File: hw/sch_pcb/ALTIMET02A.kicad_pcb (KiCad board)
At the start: 2 copper layers, 40.1 x 19.8 mm, 14 parts, among them IC1 MS561101BA03-50, J1 HEADER_2x03_PARALLEL, J2 HEADER_2x03, J3 HEADER_2x05_PARALLEL

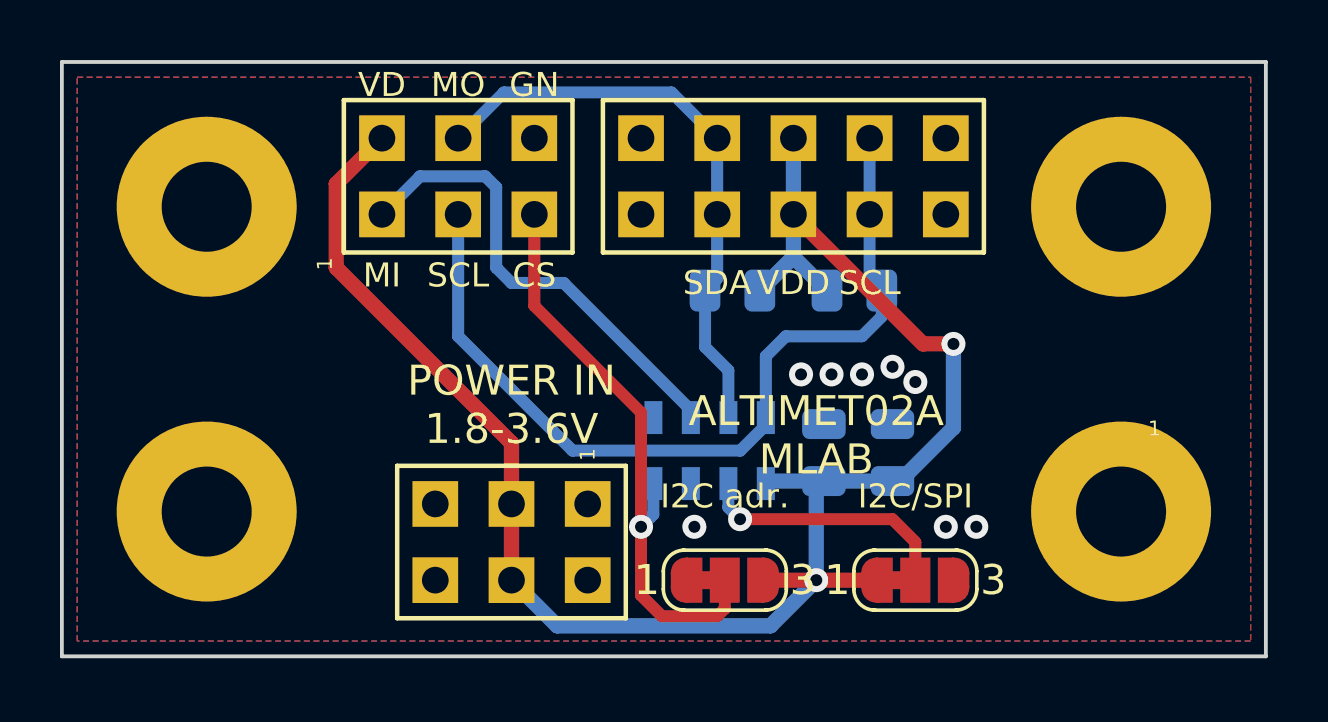
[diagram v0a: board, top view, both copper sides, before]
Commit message: Layout and silkscreen improvements.
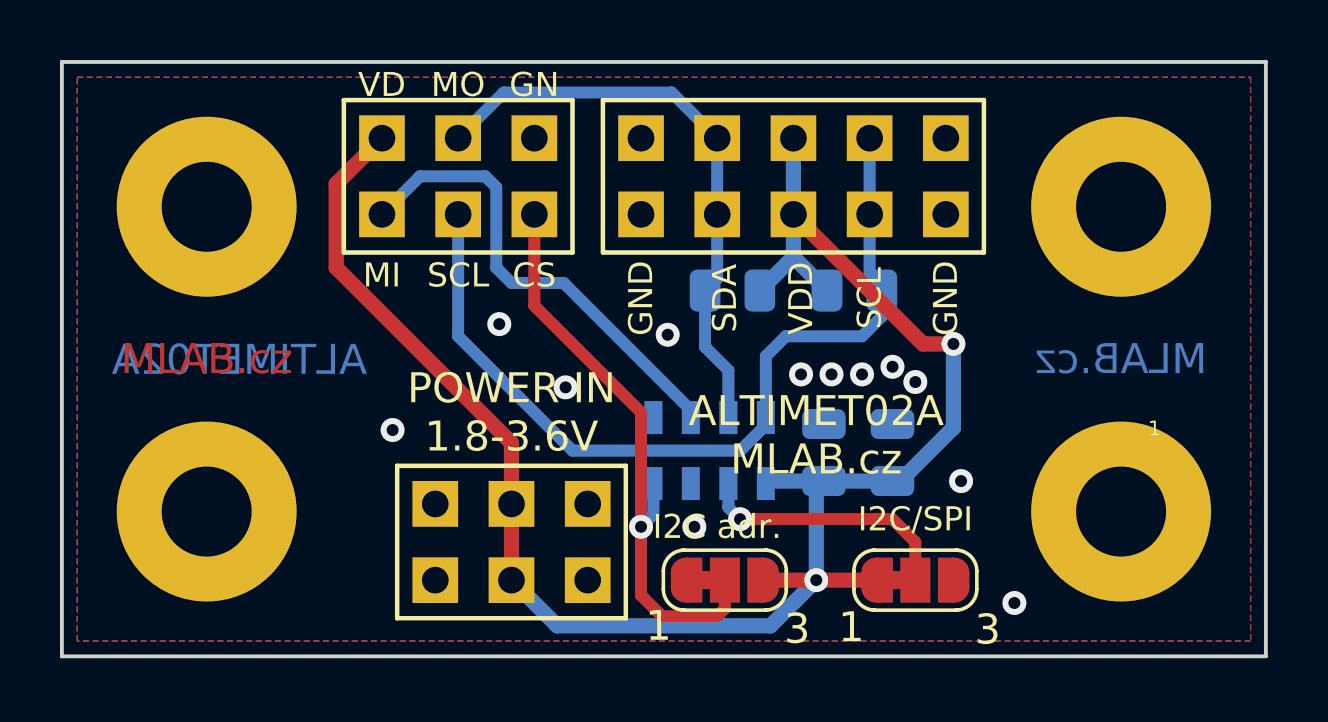
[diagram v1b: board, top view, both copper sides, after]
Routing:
- net GND: vias 8 -> 12
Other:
- board text added: "ALTIMET02A"
- board text added: "ALTIMET02A MLAB.cz"
- board text added: "GND"
- board text added: "MLAB.cz"
- board text removed: "ALTIMET02A MLAB"
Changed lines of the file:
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@@
       (effects (font (size 1.5 1.5) (thickness 0.15)))
-    )
-    (fp_text user "1" (at -2.921 -4.442928 90) (layer "F.SilkS")
-      (effects (font (size 0.5 0.5) (thickness 0.05)))
     )
     (fp_line (start -2.54 3.81) (end -2.54 -3.81) (layer "F.SilkS") (width 0.15))
@@
       (effects (font (size 1 1) (thickness 0.15)))
     )
-    (fp_text user "3" (at 2.6 0) (layer "F.SilkS")
-      (effects (font (size 1 1) (thickness 0.15)))
-    )
-    (fp_text user "1" (at -2.6 0) (layer "F.SilkS")
+    (fp_text user "3" (at 2.413 1.6256) (layer "F.SilkS")
+      (effects (font (size 1 1) (thickness 0.15)))
+    )
+    (fp_text user "1" (at -2.2098 1.524) (layer "F.SilkS")
       (effects (font (size 1 1) (thickness 0.15)))
     )
@@
       (effects (font (size 1 1) (thickness 0.15)))
     )
-    (fp_text user "1" (at -2.6 0) (layer "F.SilkS")
-      (effects (font (size 1 1) (thickness 0.15)))
-    )
-    (fp_text user "3" (at 2.6 0) (layer "F.SilkS")
+    (fp_text user "1" (at -2.1336 1.5748) (layer "F.SilkS")
+      (effects (font (size 1 1) (thickness 0.15)))
+    )
+    (fp_text user "3" (at 2.413 1.651) (layer "F.SilkS")
       (effects (font (size 1 1) (thickness 0.15)))
     )
@@
       (effects (font (size 1.5 1.5) (thickness 0.15)))
     )
-    (fp_text user "1" (at -2.921 -2.54 90) (layer "F.SilkS")
+    (fp_text user "1" (at -2.921 -2.54 90) (layer "F.SilkS") hide
       (effects (font (size 0.5 0.5) (thickness 0.05)))
     )
@@
     (property "Sheetname" "")
     (attr smd)
-    (fp_text reference "IC1" (at 0 0 90) (layer "B.SilkS")
+    (fp_text reference "IC1" (at 1.4224 -3.4036 90) (layer "B.SilkS")
       (effects (font (size 1.27 1.27) (thickness 0.254)) (justify mirror))
     )
@@
   (gr_line (start 152.146 116.586) (end 112.014 116.586) (layer "Edge.Cuts") (width 0.127))
   (gr_line (start 152.146 96.774) (end 152.146 116.586) (layer "Edge.Cuts") (width 0.127))
+  (gr_text "MLAB.cz" (at 116.84 106.68) (layer "F.Cu")
+    (effects (font (size 1 1) (thickness 0.15)))
+  )
+  (gr_text "MLAB.cz" (at 147.32 106.68) (layer "B.Cu")
+    (effects (font (size 1 1) (thickness 0.15)) (justify mirror))
+  )
+  (gr_text "ALTIMET02A" (at 117.9322 106.7054) (layer "B.Cu")
+    (effects (font (size 1 1) (thickness 0.15)) (justify mirror))
+  )
   (gr_text "GN" (at 127.762 97.536) (layer "F.SilkS")
     (effects (font (size 0.8 0.8) (thickness 0.15)))
@@
     (effects (font (size 0.8 0.8) (thickness 0.15)))
   )
-  (gr_text "SDA" (at 133.858 104.14) (layer "F.SilkS")
+  (gr_text "SDA" (at 134.112 104.648 90) (layer "F.SilkS")
     (effects (font (size 0.8 0.8) (thickness 0.15)))
   )
@@
     (effects (font (size 0.8 0.8) (thickness 0.15)))
   )
-  (gr_text "SCL" (at 138.938 104.14) (layer "F.SilkS")
-    (effects (font (size 0.8 0.8) (thickness 0.15)))
-  )
-  (gr_text "VDD" (at 136.398 104.14) (layer "F.SilkS")
-    (effects (font (size 0.8 0.8) (thickness 0.15)))
-  )
-  (gr_text "POWER IN\n1.8-3.6V" (at 127 108.204) (layer "F.SilkS")
+  (gr_text "GND" (at 141.478 104.648 90) (layer "F.SilkS")
+    (effects (font (size 0.8 0.8) (thickness 0.15)))
+  )
+  (gr_text "SCL" (at 138.938 104.648 90) (layer "F.SilkS")
+    (effects (font (size 0.8 0.8) (thickness 0.15)))
+  )
+  (gr_text "VDD" (at 136.652 104.648 90) (layer "F.SilkS")
+    (effects (font (size 0.8 0.8) (thickness 0.15)))
+  )
+  (gr_text "POWER IN\n1.8-3.6V" (at 127 108.458) (layer "F.SilkS")
     (effects (font (size 1 1) (thickness 0.15)))
   )
-  (gr_text "I2C adr." (at 134.112 111.252) (layer "F.SilkS")
+  (gr_text "I2C adr." (at 133.858 112.268) (layer "F.SilkS")
     (effects (font (size 0.8 0.8) (thickness 0.15)))
   )
@@
     (effects (font (size 0.8 0.8) (thickness 0.15)))
   )
-  (gr_text "ALTIMET02A\nMLAB" (at 137.16 109.22) (layer "F.SilkS")
+  (gr_text "GND" (at 131.318 104.648 90) (layer "F.SilkS")
+    (effects (font (size 0.8 0.8) (thickness 0.15)))
+  )
+  (gr_text "ALTIMET02A\nMLAB.cz" (at 137.16 109.22) (layer "F.SilkS")
     (effects (font (size 1 1) (thickness 0.15)))
   )
@@
     (effects (font (size 0.8 0.8) (thickness 0.15)))
   )
-  (gr_text "I2C/SPI" (at 140.462 111.252) (layer "F.SilkS")
+  (gr_text "I2C/SPI" (at 140.462 112.014) (layer "F.SilkS")
     (effects (font (size 0.8 0.8) (thickness 0.15)))
   )
@@
   (segment (start 134.229 111.623) (end 134.229 110.828) (width 0.4) (layer "B.Cu") (net 5))
   (segment (start 134.62 112.014) (end 134.229 111.623) (width 0.4) (layer "B.Cu") (net 5))
-  (via (at 142.494 112.268) (size 0.8) (drill 0.4) (layers "F.Cu" "B.Cu") (free) (net 6))
+  (via (at 126.5936 105.5116) (size 0.8) (drill 0.4) (layers "F.Cu" "B.Cu") (free) (net 6))
+  (via (at 123.0376 109.0422) (size 0.8) (drill 0.4) (layers "F.Cu" "B.Cu") (free) (net 6))
+  (via (at 141.986 110.744) (size 0.8) (drill 0.4) (layers "F.Cu" "B.Cu") (free) (net 6))
+  (via (at 128.8034 107.6198) (size 0.8) (drill 0.4) (layers "F.Cu" "B.Cu") (free) (net 6))
   (via (at 133.096 112.268) (size 0.8) (drill 0.4) (layers "F.Cu" "B.Cu") (free) (net 6))
   (via (at 136.652 107.188) (size 0.8) (drill 0.4) (layers "F.Cu" "B.Cu") (free) (net 6))
   (via (at 140.462 107.442) (size 0.8) (drill 0.4) (layers "F.Cu" "B.Cu") (free) (net 6))
+  (via (at 132.207 105.8672) (size 0.8) (drill 0.4) (layers "F.Cu" "B.Cu") (free) (net 6))
   (via (at 138.684 107.188) (size 0.8) (drill 0.4) (layers "F.Cu" "B.Cu") (free) (net 6))
   (via (at 137.668 107.188) (size 0.8) (drill 0.4) (layers "F.Cu" "B.Cu") (free) (net 6))
-  (via (at 141.478 112.268) (size 0.8) (drill 0.4) (layers "F.Cu" "B.Cu") (free) (net 6))
+  (via (at 143.764 114.808) (size 0.8) (drill 0.4) (layers "F.Cu" "B.Cu") (free) (net 6))
   (via (at 139.7 106.934) (size 0.8) (drill 0.4) (layers "F.Cu" "B.Cu") (free) (net 6))
   (segment (start 139.3425 105.2595) (end 138.684 105.918) (width 0.4) (layer "B.Cu") (net 7))

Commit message: power header deleted, i2c/spi solder jumper moved to the back side, i2c addr. added
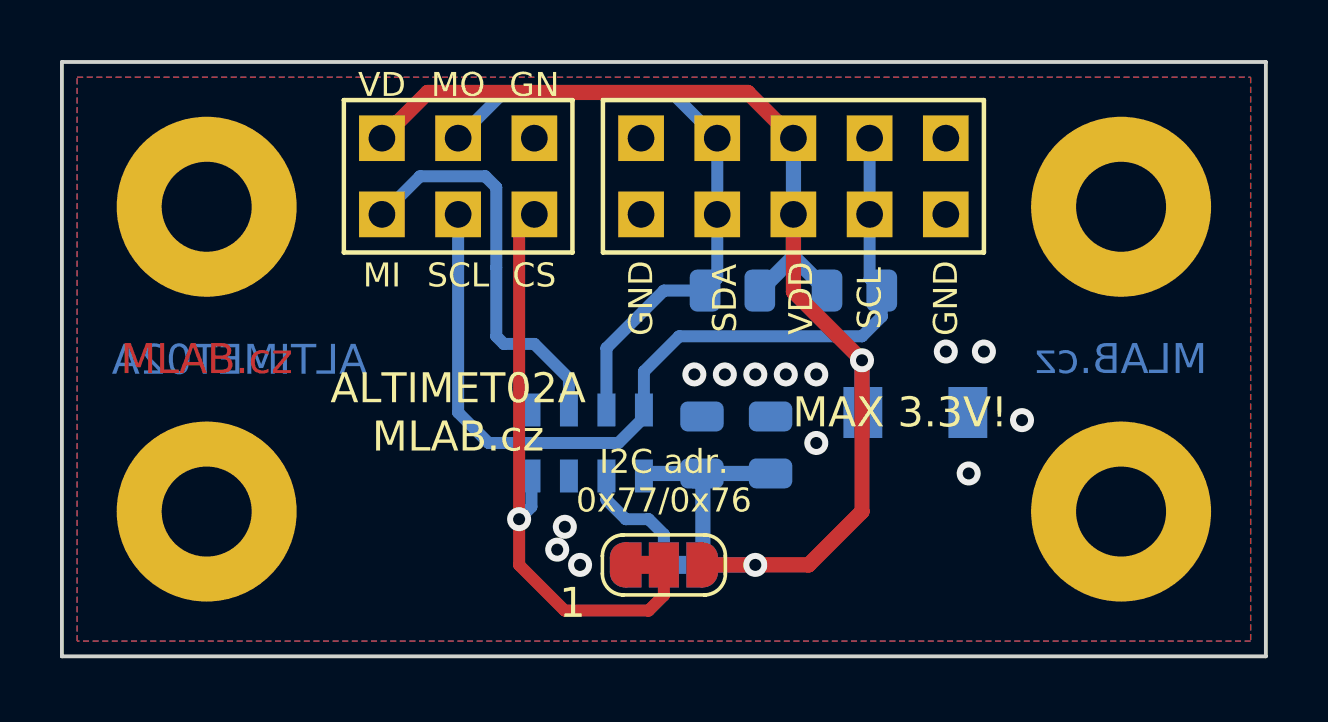
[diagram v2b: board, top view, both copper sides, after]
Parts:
- removed J1: HEADER_2x03_PARALLEL, Mlab_Pin_Headers:Straight_2x03
- added D1: BZV55C3V6, Mlab_D:Diode-MiniMELF_Standard, B.Cu at (140.5, 108.5)
- JP1: moved to B.Cu
- moved JP1 8.40 mm to (132.1, 113.5), turned to 180 degrees
- moved IC1 4.07 mm to (129.5, 109.5)
- moved C1 4.07 mm to (133.3, 109.5)
- moved C2 4.07 mm to (135.6, 109.5)
- moved JP3 2.09 mm to (132.1, 113.5)
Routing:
- net VDD: track 60.4 -> 50.4 mm
- net /PS: track 8.78 -> 4.20 mm, vias 1 -> 0
- net MISO: track 16.1 -> 14.0 mm
- net MOSI/SDA: track 19.7 -> 21.3 mm
- net SCLK: track 29.1 -> 29.9 mm
- net GND: vias 12 -> 13
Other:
- board text added: "I2C adr. 0x77/0x76"
- board text added: "MAX 3.3V!"
- board text removed: "I2C adr."
- board text removed: "POWER IN 1.8-3.6V"

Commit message: Improve layout and silkscreen.
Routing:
- net MISO: track 14.0 -> 13.4 mm
- net GND: vias 13 -> 14
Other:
- board text added: "ALTIMET02A MLAB.cz 2023"
- board text removed: "ALTIMET02A MLAB.cz"
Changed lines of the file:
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@@
-      (effects (font (size 1 1) (thickness 0.15)))
-    )
-    (fp_text user "1" (at -3.048 1.27) (layer "F.SilkS")
       (effects (font (size 1 1) (thickness 0.15)))
     )
@@
     (effects (font (size 0.8 0.8) (thickness 0.15)))
   )
-  (gr_text "ALTIMET02A\nMLAB.cz" (at 125.222 108.458) (layer "F.SilkS")
+  (gr_text "ALTIMET02A\nMLAB.cz\n2023" (at 125.222 108.458) (layer "F.SilkS")
     (effects (font (size 1 1) (thickness 0.15)))
   )
@@
   (gr_text "MI" (at 122.682 103.886) (layer "F.SilkS")
     (effects (font (size 0.8 0.8) (thickness 0.15)))
+  )
+  (dimension (type aligned) (layer "Cmts.User")
+    (pts (xy 152.146 116.586) (xy 152.146 96.774))
+    (height 8.89)
+    (gr_text "780 mils" (at 159.886 106.68 90) (layer "Cmts.User")
+      (effects (font (size 1 1) (thickness 0.15)))
+    )
+    (format (units 3) (units_format 1) (precision 4) suppress_zeroes)
+    (style (thickness 0.15) (arrow_length 1.27) (text_position_mode 0) (extension_height 0.58642) (extension_offset 0.5) keep_text_aligned)
+  )
+  (dimension (type aligned) (layer "Cmts.User")
+    (pts (xy 116.84 101.6) (xy 147.32 101.6))
+    (height -7.874)
+    (gr_text "1200 mils" (at 132.08 92.576) (layer "Cmts.User")
+      (effects (font (size 1 1) (thickness 0.15)))
+    )
+    (format (units 3) (units_format 1) (precision 4) suppress_zeroes)
+    (style (thickness 0.15) (arrow_length 1.27) (text_position_mode 0) (extension_height 0.58642) (extension_offset 0.5) keep_text_aligned)
+  )
+  (dimension (type aligned) (layer "Cmts.User")
+    (pts (xy 147.32 111.76) (xy 147.32 101.6))
+    (height 9.398)
+    (gr_text "400 mils" (at 155.568 106.68 90) (layer "Cmts.User")
+      (effects (font (size 1 1) (thickness 0.15)))
+    )
+    (format (units 3) (units_format 1) (precision 4) suppress_zeroes)
+    (style (thickness 0.15) (arrow_length 1.27) (text_position_mode 0) (extension_height 0.58642) (extension_offset 0.5) keep_text_aligned)
+  )
+  (dimension (type aligned) (layer "Cmts.User")
+    (pts (xy 112.014 96.774) (xy 152.146 96.774))
+    (height -6.858)
+    (gr_text "1580 mils" (at 132.08 88.766) (layer "Cmts.User")
+      (effects (font (size 1 1) (thickness 0.15)))
+    )
+    (format (units 3) (units_format 1) (precision 4) suppress_zeroes)
+    (style (thickness 0.15) (arrow_length 1.27) (text_position_mode 0) (extension_height 0.58642) (extension_offset 0.5) keep_text_aligned)
   )
   (segment (start 136.398 104.4315) (end 138.684 106.7175) (width 0.508) (layer "F.Cu") (net 1))
@@
   (segment (start 133.858 99.314) (end 132.334 97.79) (width 0.4) (layer "B.Cu") (net 2))
   (segment (start 133.4535 104.394) (end 132.08 104.394) (width 0.4) (layer "B.Cu") (net 2))
-  (segment (start 126.746 106.172) (end 126.492 105.918) (width 0.4) (layer "B.Cu") (net 3))
-  (segment (start 126.492 103.632) (end 126.492 100.95) (width 0.4) (layer "B.Cu") (net 3))
-  (segment (start 126.492 105.918) (end 126.492 103.632) (width 0.4) (layer "B.Cu") (net 3))
+  (segment (start 123.952 100.584) (end 122.682 101.854) (width 0.4) (layer "B.Cu") (net 3))
+  (segment (start 126.492 100.95) (end 126.126 100.584) (width 0.4) (layer "B.Cu") (net 3))
+  (segment (start 126.492 104.902) (end 126.492 100.95) (width 0.4) (layer "B.Cu") (net 3))
+  (segment (start 128.915 107.325) (end 126.492 104.902) (width 0.4) (layer "B.Cu") (net 3))
+  (segment (start 128.915 108.374) (end 128.915 108.124) (width 0.4) (layer "B.Cu") (net 3))
+  (segment (start 126.126 100.584) (end 123.952 100.584) (width 0.4) (layer "B.Cu") (net 3))
   (segment (start 128.915 108.374) (end 128.915 107.325) (width 0.4) (layer "B.Cu") (net 3))
-  (segment (start 128.915 108.374) (end 128.915 108.124) (width 0.4) (layer "B.Cu") (net 3))
-  (segment (start 128.915 107.325) (end 127.762 106.172) (width 0.4) (layer "B.Cu") (net 3))
-  (segment (start 126.492 100.95) (end 126.126 100.584) (width 0.4) (layer "B.Cu") (net 3))
-  (segment (start 123.952 100.584) (end 122.682 101.854) (width 0.4) (layer "B.Cu") (net 3))
   (segment (start 128.915 108.374) (end 128.915 108.624) (width 0.25) (layer "B.Cu") (net 3))
-  (segment (start 126.126 100.584) (end 123.952 100.584) (width 0.4) (layer "B.Cu") (net 3))
-  (segment (start 127.762 106.172) (end 126.746 106.172) (width 0.4) (layer "B.Cu") (net 3))
   (segment (start 132.08 113.538) (end 132.08 114.554) (width 0.4) (layer "F.Cu") (net 4))
   (segment (start 127.254 112.014) (end 127.254 102.362) (width 0.4) (layer "F.Cu") (net 4))
@@
   (via (at 137.16 107.188) (size 0.8) (drill 0.4) (layers "F.Cu" "B.Cu") (free) (net 6))
   (via (at 129.286 113.538) (size 0.8) (drill 0.4) (layers "F.Cu" "B.Cu") (free) (net 6))
+  (via (at 129.286 104.648) (size 0.8) (drill 0.4) (layers "F.Cu" "B.Cu") (free) (net 6))
   (via (at 142.24 110.49) (size 0.8) (drill 0.4) (layers "F.Cu" "B.Cu") (free) (net 6))
   (via (at 137.16 109.474) (size 0.8) (drill 0.4) (layers "F.Cu" "B.Cu") (free) (net 6))
   (via (at 142.748 106.426) (size 0.8) (drill 0.4) (layers "F.Cu" "B.Cu") (free) (net 6))
-  (via (at 128.778 112.268) (size 0.8) (drill 0.4) (layers "F.Cu" "B.Cu") (free) (net 6))
+  (via (at 129.286 112.268) (size 0.8) (drill 0.4) (layers "F.Cu" "B.Cu") (free) (net 6))
   (via (at 133.096 107.188) (size 0.8) (drill 0.4) (layers "F.Cu" "B.Cu") (free) (net 6))
   (via (at 144.018 108.712) (size 0.8) (drill 0.4) (layers "F.Cu" "B.Cu") (free) (net 6))
